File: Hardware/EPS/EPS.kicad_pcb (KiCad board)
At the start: 4 copper layers, 85 x 85 mm, 114 parts, among them J1001 Conn_01x02, J101 Conn_02x02_Odd_Even, J1101 Conn_01x02, J201 Conn_ARM_JTAG_SWD_10, J301 Conn_02x02_Counter_Clockwise, J401 USB_C_Receptacle_PowerOnly_6P, J601 Conn_02x20_Odd_Even, J701 Conn_01x02, J801 Conn_01x02, J901 Conn_01x02, M1201 MountingHole_Pad, M1202 MountingHole_Pad, M1203 MountingHole_Pad, M1204 MountingHole_Pad, Q301 RQ3G100GNTB, Q302 RQ3G100GNTB, U201 STM32L431RCT, U202 HZ0805E601R-10, U301 LTC4162EUFD-L41#PBF, U401 NCP176AMX330TCG, U501 RT8258GE, U502 TPS27081ADDCR, U503 RT8258GE, U504 B230A-13-F

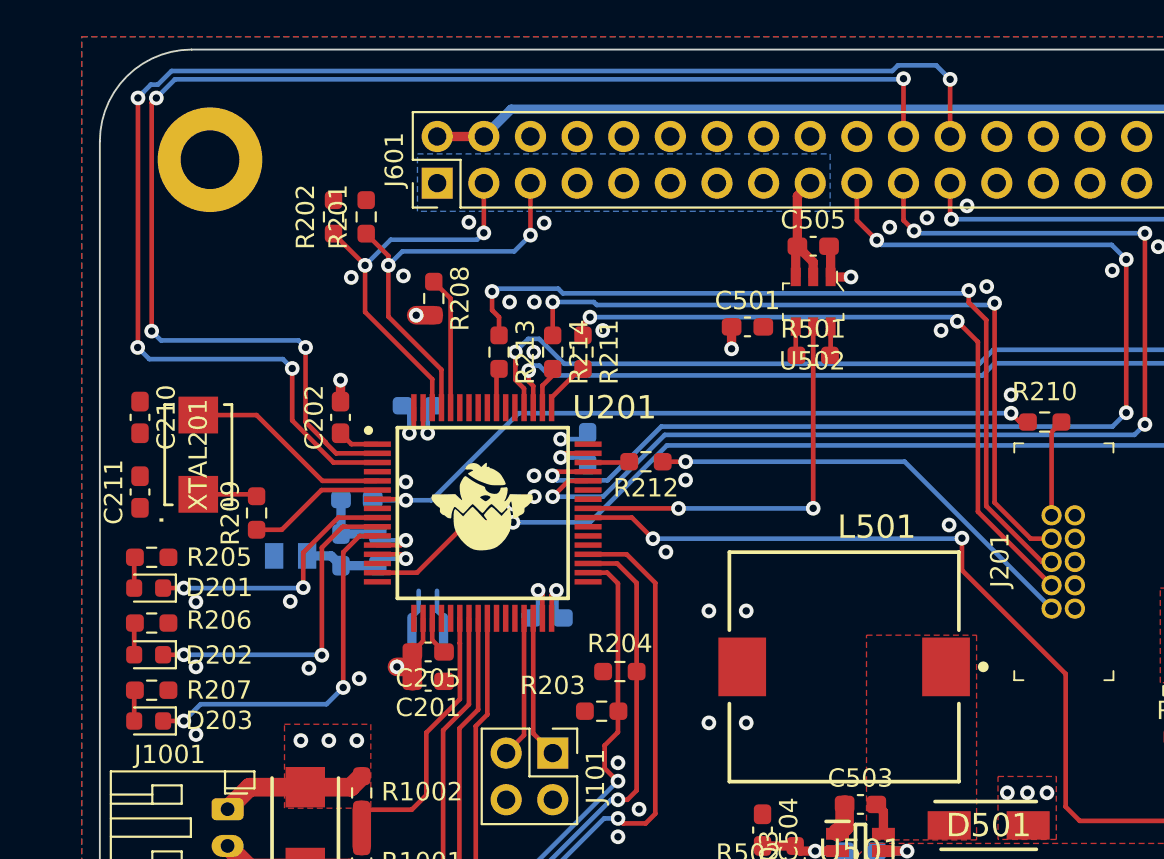
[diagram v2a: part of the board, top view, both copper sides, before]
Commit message: Finished XTAL layout
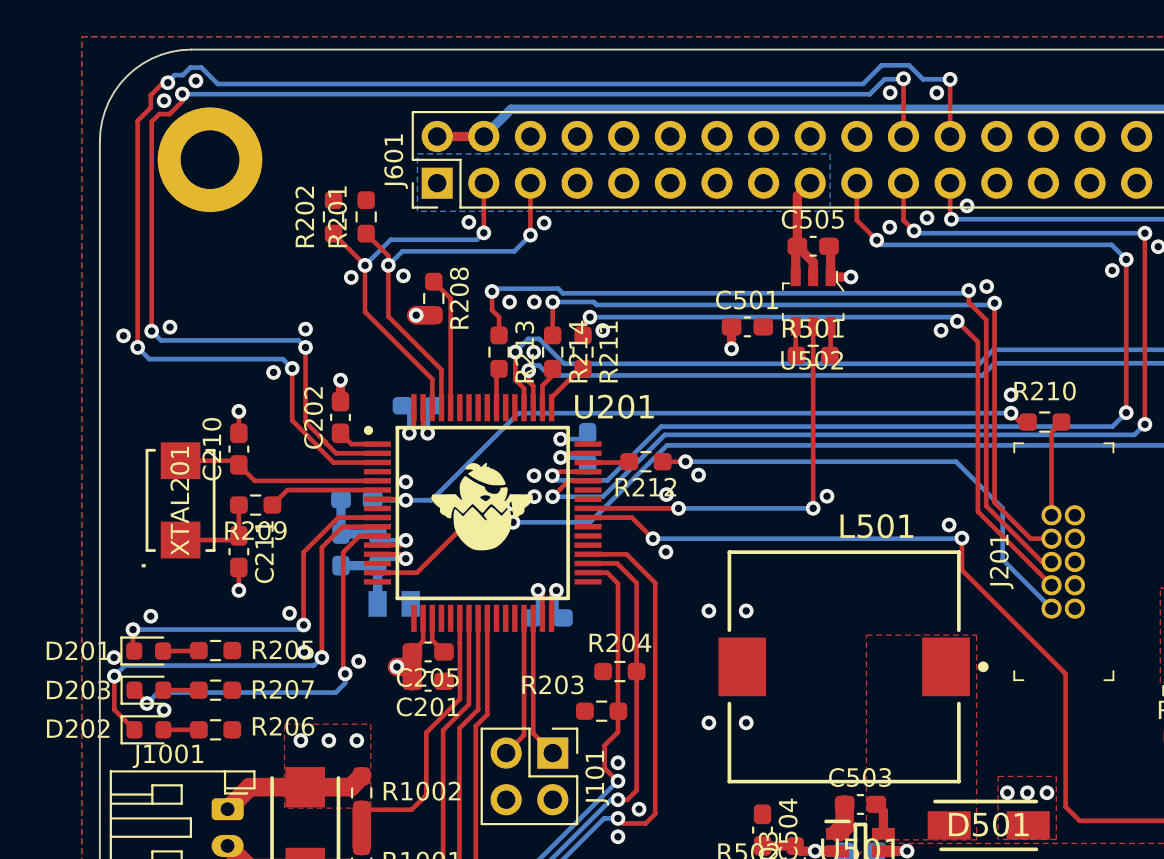
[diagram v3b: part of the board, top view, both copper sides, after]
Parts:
- added G***: LOGO, LOGO, B.Cu at (161.0, 131.9)
- moved G003 91.8 mm to (251.3, 104.2)
- moved R206 6.78 mm to (115.4, 97.4)
- moved C211 6.29 mm to (116.6, 87.7), turned to -90 degrees
- moved U202 6.22 mm to (125.1, 90.6), turned to 180 degrees
- moved R205 6.16 mm to (115.4, 93.1)
- moved C210 5.66 mm to (116.6, 82.1), turned to 90 degrees
- moved D202 4.09 mm to (111.7, 97.4), turned to 0 degrees
- moved R207 3.48 mm to (115.4, 95.2)
- moved D201 3.43 mm to (111.7, 93.1), turned to 0 degrees
- moved XTAL201 2.67 mm to (113.5, 84.9)
- moved D203 1.68 mm to (111.7, 95.2), turned to 0 degrees
- moved R209 0.43 mm to (117.6, 85.2), turned to 180 degrees
- turned G001 to -90 degrees
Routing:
- net /STM32 MCU/LED_G: track 18.0 -> 24.6 mm
- net /STM32 MCU/LED_R: track 14.4 -> 19.4 mm
- net +3.3V: track 17.3 -> 14.0 mm
- net Net-(C211-Pad1): track 3.22 -> 4.95 mm
- net Net-(J201-Pad2): track 24.5 -> 26.1 mm
- net /STM32 MCU/LED_YL: track 20.2 -> 21.7 mm
- net /STM32 MCU/HSE_OUT: track 7.48 -> 6.06 mm
- net GND: track 59.8 -> 59.1 mm, vias 88 -> 100

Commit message: Finished EPS - v0.1.0
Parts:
- removed G003: LOGO, LOGO
- added D102: BZT585B24T-7, Diode_SMD:D_SOD-523, F.Cu at (137.7, 119.2)
- added G***: LOGO, LOGO, F.Cu at (155.1, 63.0)
- added G***: LOGO, LOGO, F.Cu at (130.3, 70.2)
- added G***: LOGO, LOGO, F.Cu at (150.6, 70.2)
- added G***: LOGO, LOGO, F.Cu at (173.5, 70.2)
- added G***: LOGO, LOGO, F.Cu at (170.9, 70.2)
- added G***: LOGO, LOGO, F.Cu at (152.5, 63.0)
- added G***: LOGO, LOGO, F.Cu at (155.7, 70.2)
- added G***: LOGO, LOGO, F.Cu at (153.2, 70.2)
- added G***: LOGO, LOGO, F.Cu at (132.8, 70.2)
- C209, C301, C303: value 0.1uF -> 100nF
- C401, C402: value 1uF -> 4.7uF
- M1201, M1202, M1203, M1204: footprint MountingHole:MountingHole_3.2mm_M3_ISO7380_Pad -> MountingHole:MountingHole_3.2mm_M3_Pad_Via
- U201: footprint STM32L431RCT6:QFP50P1200X1200X160-64N -> STM32L431RCT:LQFP-64
- U401: value NCP176AMX330TCG -> AP7361C-33Y5-13; footprint NCP176AMX330TCG:NCP176AMX330TCG -> AP7361C-25Y5-13:AP7361C25Y513
- XTAL201: footprint NX5032GA-8.000M:XTAL_NX5032_NDK-M -> NX5032GA-8.000M:XTAL_NX5032_NDK
- moved G002 41.4 mm to (122.9, 115.8), turned to 180 degrees
- moved U401 8.00 mm to (178.4, 74.4), turned to 90 degrees
- moved C402 8.00 mm to (175.0, 75.2), turned to 90 degrees
- moved C401 7.45 mm to (181.9, 75.2), turned to 90 degrees
- moved R402 2.08 mm to (183.6, 81.8), turned to 180 degrees
- moved R401 2.05 mm to (183.6, 80.0), turned to 180 degrees
- moved U202 1.83 mm to (123.3, 90.9), turned to 0 degrees
- moved D401 0.18 mm to (187.7, 88.8)
- moved R204 0.10 mm to (137.3, 94.2)
- turned G001 to 180 degrees
- renumbered G*** to G002
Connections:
- C401 pad 1: GND -> /USB Power/USB_VBUS
- C401 pad 2: /USB Power/USB_VBUS -> GND
- J601 pad 32: /Board Connector/PIN_32 -> unconnected-(J601-Pad32)
- J601 pad 36: /Board Connector/PIN_36 -> unconnected-(J601-Pad36)
- U401 pad 1: +3.3V -> /USB Power/USB_VBUS
- U401 pad 2: +3.3V -> GND
- U401 pad 3: GND -> unconnected-(U401-Pad3)
- U401 pad 5: unconnected-(U401-Pad5) -> +3.3V
- U401 pad 6: /USB Power/USB_VBUS -> GND
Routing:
- net /USB Power/USB_VBUS: track 13.3 -> 39.4 mm
- net GND: track 59.1 -> 75.3 mm, vias 100 -> 116
- net Net-(J401-PadB5): track 0.00 -> 3.20 mm
- net Net-(J401-PadA5): track 0.00 -> 3.20 mm
- net +3.3V: track 14.0 -> 16.0 mm
- net /GPIO_13: track 74.2 -> 75.3 mm
- net /GPIO_14: track 79.8 -> 80.3 mm
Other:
- board text added: "GPIO"
- board text added: "RX"
- board text added: "SCK"
- board text added: "SCL"
- board text added: "SDA"
- board text added: "SDI"
- board text added: "SDO"
- board text added: "TX"
